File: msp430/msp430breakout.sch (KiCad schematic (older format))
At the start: 18 parts, among them P1 Power, T1 Crystal_Small, X1 Power, X2 Power, X3 Left, X4 Power, X5 Power, X6 Right, X7 Debug

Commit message: a bit of work on the layout
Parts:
- removed X3: Left, Connector_PinHeader_2.54mm:PinHeader_1x06_P2.54mm_Vertical, symbol Connector:Conn_01x06_Male
- removed X6: Right, Connector_PinHeader_2.54mm:PinHeader_1x06_P2.54mm_Vertical, symbol Connector:Conn_01x06_Male
- added X3: Left, Connector_PinHeader_2.54mm:PinHeader_1x05_P2.54mm_Vertical, symbol Connector:Conn_01x05_Male
- added X6: Right, Connector_PinHeader_2.54mm:PinHeader_1x05_P2.54mm_Vertical, symbol Connector:Conn_01x05_Male
- added X8: PWR_L_OOL, Connector_PinHeader_2.54mm:PinHeader_2x02_P2.54mm_Vertical, symbol Connector:Conn_01x04_Male
- added X9: PWR_R_OOL, Connector_PinHeader_2.54mm:PinHeader_2x02_P2.54mm_Vertical, symbol Connector:Conn_01x04_Male
- X7: footprint Connector_Molex:Molex_Micro-Latch_53253-0370_1x03_P2.00mm_Vertical -> Connector_PinHeader_2.54mm:PinHeader_1x03_P2.54mm_Vertical
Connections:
- wire segments 47 -> 79
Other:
- moved on the sheet: X1, X2, X4, X5

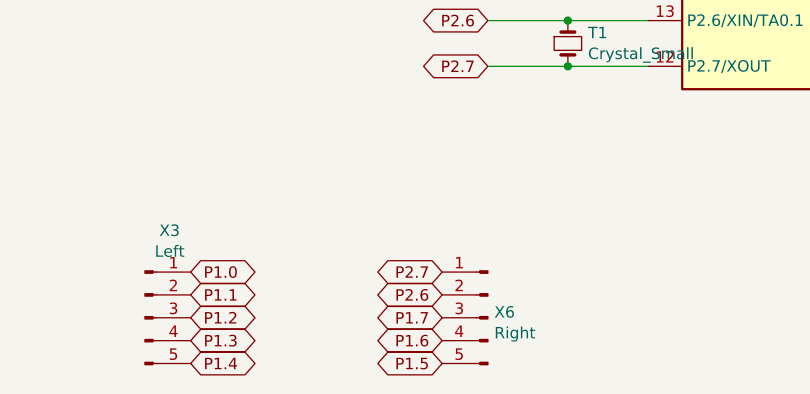
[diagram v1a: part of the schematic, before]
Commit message: increased board size to have planes go around pin headers
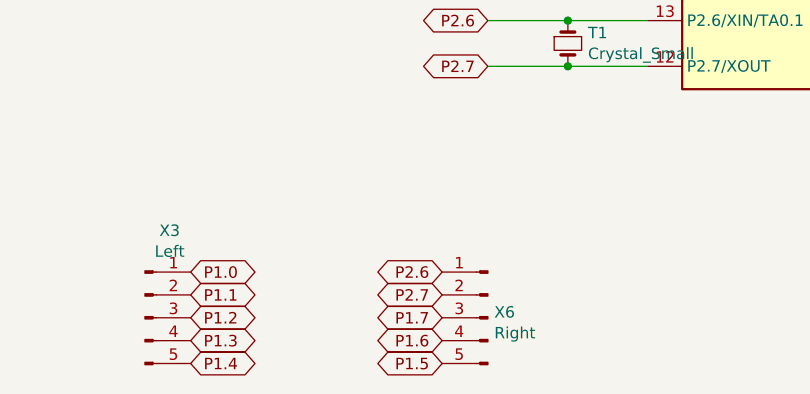
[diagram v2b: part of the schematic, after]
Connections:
- net P2.6: now also X6.1 (Pin_1); no longer X6.2 (Pin_2)
- net P2.7: now also X6.2 (Pin_2); no longer X6.1 (Pin_1)
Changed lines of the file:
@@
 Text GLabel 3300 6500 0    50   BiDi ~ 0
 P1.7
+Text GLabel 3300 6300 0    50   BiDi ~ 0
+P2.6
 Text GLabel 3300 6400 0    50   BiDi ~ 0
-P2.6
-Text GLabel 3300 6300 0    50   BiDi ~ 0
 P2.7
 Text GLabel 5800 4550 2    50   Input ~ 0

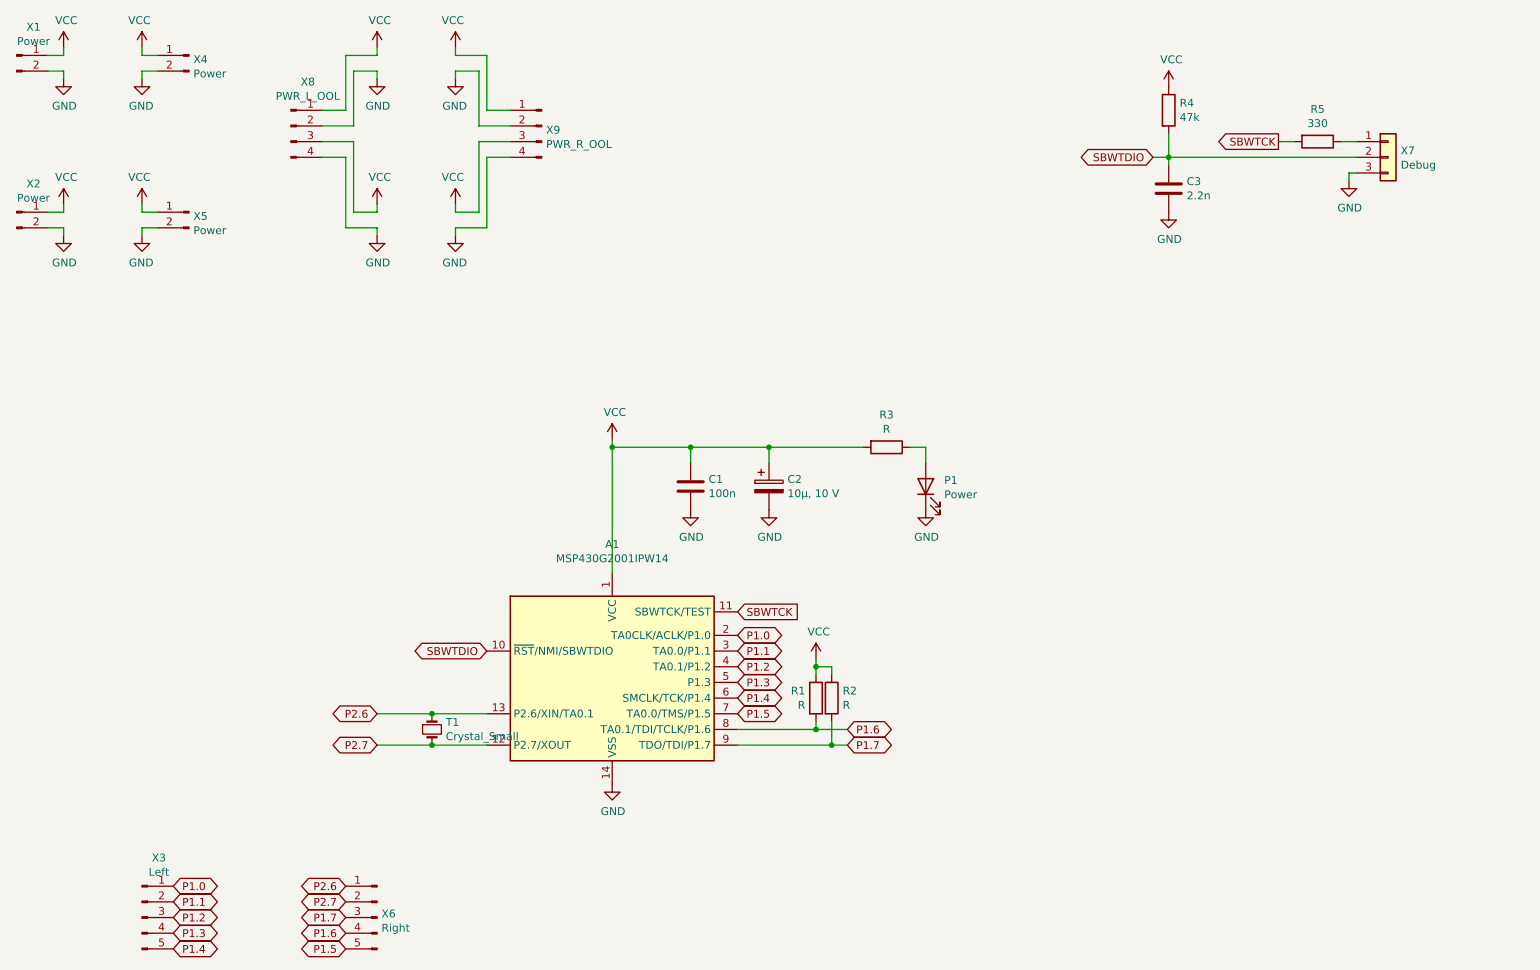
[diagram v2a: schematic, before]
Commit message: added linear regulator
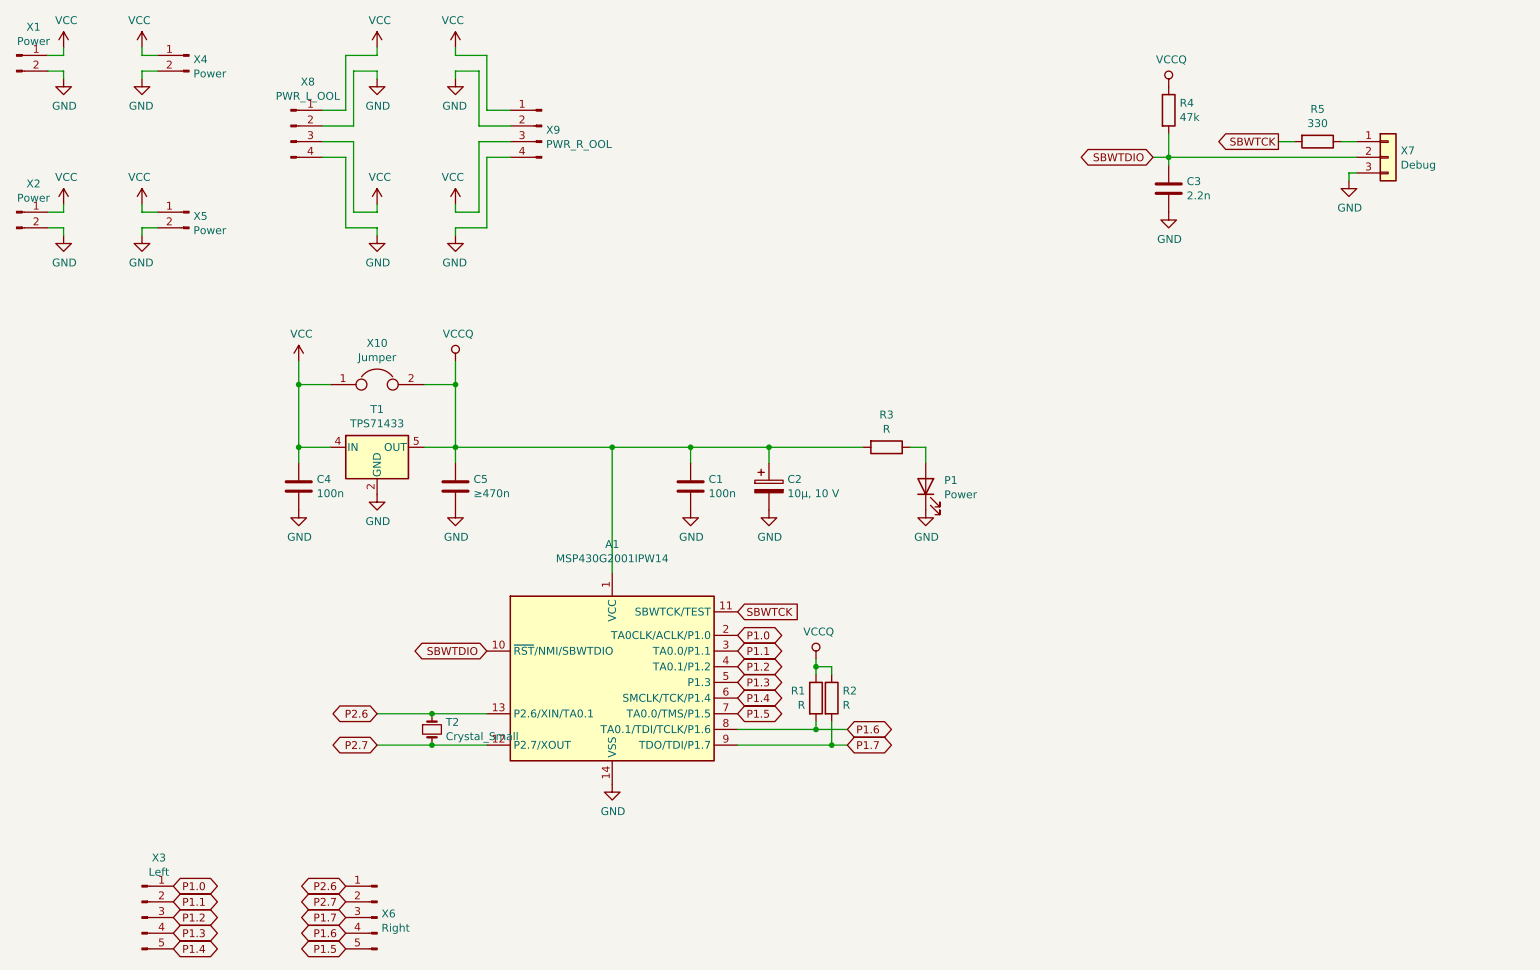
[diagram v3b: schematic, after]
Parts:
- added C4: 100n, Capacitor_SMD:C_0805_2012Metric_Pad1.15x1.40mm_HandSolder, symbol Device:C
- added C5: ≥470n, Capacitor_SMD:C_0805_2012Metric_Pad1.15x1.40mm_HandSolder, symbol Device:C
- added T1: TPS71433, Package_TO_SOT_SMD:SOT-353_SC-70-5, symbol Regulator_Linear:TPS71533__SC70
- added X10: Jumper, symbol Device:Jumper
- renumbered T1 to T2
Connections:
- net GND: now also C4.2, C5.2, T1.2 (GND)
- net VCC: now also C4.1, T1.4 (IN), X10.1; no longer A1.1 (VCC), C1.1, C2.1, R1.1, R2.1, R3.2, R4.1
- new net VCCQ: A1.1 (VCC), C1.1, C2.1, C5.1, R1.1, R2.1, R3.2, R4.1, T1.5 (OUT), X10.2
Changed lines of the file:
@@
-	1    0    0    -1
-$EndComp
-Connection ~ 5000 3500
-Wire Wire Line
-	5000 3450 5000 3500
-$Comp
-L power:VCC #PWR0103
-U 1 1 5E4D6472
-P 5000 3450
-F 0 "#PWR0103" H 5000 3300 50  0001 C CNN
-F 1 "VCC" H 5017 3623 50  0000 C CNN
-F 2 "" H 5000 3450 50  0001 C CNN
-F 3 "" H 5000 3450 50  0001 C CNN
-	1    5000 3450
 	1    0    0    -1
 $EndComp
@@
 	6300 4900 6300 4850
 Connection ~ 6300 4900
-$Comp
-L power:VCC #PWR0116
-U 1 1 5E4EBDF5
-P 6300 4850
-F 0 "#PWR0116" H 6300 4700 50  0001 C CNN
-F 1 "VCC" H 6317 5023 50  0000 C CNN
-F 2 "" H 6300 4850 50  0001 C CNN
-F 3 "" H 6300 4850 50  0001 C CNN
-	1    6300 4850
-	1    0    0    -1
-$EndComp
 Wire Wire Line
 	9350 1550 9250 1550
-$Comp
-L power:VCC #PWR0117
-U 1 1 5E4F1295
-P 8550 1200
-F 0 "#PWR0117" H 8550 1050 50  0001 C CNN
-F 1 "VCC" H 8567 1373 50  0000 C CNN
-F 2 "" H 8550 1200 50  0001 C CNN
-F 3 "" H 8550 1200 50  0001 C CNN
-	1    8550 1200
-	1    0    0    -1
-$EndComp
 Wire Wire Line
 	8450 1650 8550 1650
@@
 	8550 1650 9750 1650
 $Comp
-L Device:Crystal_Small T1
+L Device:Crystal_Small T2
 U 1 1 5E4F5798
 P 3850 5300
-F 0 "T1" V 3804 5388 50  0000 L CNN
+F 0 "T2" V 3804 5388 50  0000 L CNN
 F 1 "Crystal_Small" V 3895 5388 50  0000 L CNN
 F 2 "" H 3850 5300 50  0001 C CNN
@@
 	-1   0    0    -1
 $EndComp
+$Comp
+L Regulator_Linear:TPS71533__SC70 T1
+U 1 1 5E4FAA2B
+P 3500 3500
+F 0 "T1" H 3500 3742 50  0000 C CNN
+F 1 "TPS71433" H 3500 3651 50  0000 C CNN
+F 2 "Package_TO_SOT_SMD:SOT-353_SC-70-5" H 3500 3725 50  0001 C CNN
+F 3 "http://www.ti.com/lit/ds/symlink/tps715.pdf" H 3200 4300 50  0001 C CNN
+	1    3500 3500
+	1    0    0    -1
+$EndComp
+$Comp
+L power:GND #PWR0103
+U 1 1 5E4FBEB1
+P 3500 3800
+F 0 "#PWR0103" H 3500 3550 50  0001 C CNN
+F 1 "GND" H 3505 3627 50  0000 C CNN
+F 2 "" H 3500 3800 50  0001 C CNN
+F 3 "" H 3500 3800 50  0001 C CNN
+	1    3500 3800
+	1    0    0    -1
+$EndComp
+$Comp
+L Device:C C4
+U 1 1 5E4FC63E
+P 3000 3750
+F 0 "C4" H 3115 3796 50  0000 L CNN
+F 1 "100n" H 3115 3705 50  0000 L CNN
+F 2 "Capacitor_SMD:C_0805_2012Metric_Pad1.15x1.40mm_HandSolder" H 3038 3600 50  0001 C CNN
+F 3 "~" H 3000 3750 50  0001 C CNN
+	1    3000 3750
+	1    0    0    -1
+$EndComp
+$Comp
+L Device:C C5
+U 1 1 5E4FCCBF
+P 4000 3750
+F 0 "C5" H 4115 3796 50  0000 L CNN
+F 1 "≥470n" H 4115 3705 50  0000 L CNN
+F 2 "Capacitor_SMD:C_0805_2012Metric_Pad1.15x1.40mm_HandSolder" H 4038 3600 50  0001 C CNN
+F 3 "~" H 4000 3750 50  0001 C CNN
+	1    4000 3750
+	1    0    0    -1
+$EndComp
+Wire Wire Line
+	3800 3500 4000 3500
+Wire Wire Line
+	4000 3500 4000 3600
+Wire Wire Line
+	3200 3500 3000 3500
+Wire Wire Line
+	3000 3500 3000 3600
+$Comp
+L power:GND #PWR0126
+U 1 1 5E5010F7
+P 3000 3900
+F 0 "#PWR0126" H 3000 3650 50  0001 C CNN
+F 1 "GND" H 3005 3727 50  0000 C CNN
+F 2 "" H 3000 3900 50  0001 C CNN
+F 3 "" H 3000 3900 50  0001 C CNN
+	1    3000 3900
+	1    0    0    -1
+$EndComp
+$Comp
+L power:GND #PWR0127
+U 1 1 5E501339
+P 4000 3900
+F 0 "#PWR0127" H 4000 3650 50  0001 C CNN
+F 1 "GND" H 4005 3727 50  0000 C CNN
+F 2 "" H 4000 3900 50  0001 C CNN
+F 3 "" H 4000 3900 50  0001 C CNN
+	1    4000 3900
+	1    0    0    -1
+$EndComp
+$Comp
+L power:VCC #PWR0128
+U 1 1 5E503C52
+P 3000 2950
+F 0 "#PWR0128" H 3000 2800 50  0001 C CNN
+F 1 "VCC" H 3017 3123 50  0000 C CNN
+F 2 "" H 3000 2950 50  0001 C CNN
+F 3 "" H 3000 2950 50  0001 C CNN
+	1    3000 2950
+	1    0    0    -1
+$EndComp
+Connection ~ 3000 3500
+Wire Wire Line
+	4000 3500 5000 3500
+Connection ~ 4000 3500
+Connection ~ 5000 3500
+Wire Wire Line
+	3000 2950 3000 3100
+$Comp
+L Device:Jumper X10
+U 1 1 5E50AFA6
+P 3500 3100
+F 0 "X10" H 3500 3364 50  0000 C CNN
+F 1 "Jumper" H 3500 3273 50  0000 C CNN
+F 2 "" H 3500 3100 50  0001 C CNN
+F 3 "~" H 3500 3100 50  0001 C CNN
+	1    3500 3100
+	1    0    0    -1
+$EndComp
+Wire Wire Line
+	3200 3100 3000 3100
+Connection ~ 3000 3100
+Wire Wire Line
+	3000 3100 3000 3500
+Wire Wire Line
+	3800 3100 4000 3100
+Wire Wire Line
+	4000 3100 4000 3500
+Wire Wire Line
+	4000 2950 4000 3100
+Connection ~ 4000 3100
+$Comp
+L power:VCCQ #PWR0129
+U 1 1 5E577B5D
+P 4000 2950
+F 0 "#PWR0129" H 4000 2800 50  0001 C CNN
+F 1 "VCCQ" H 4017 3123 50  0000 C CNN
+F 2 "" H 4000 2950 50  0001 C CNN
+F 3 "" H 4000 2950 50  0001 C CNN
+	1    4000 2950
+	1    0    0    -1
+$EndComp
+$Comp
+L power:VCCQ #PWR0117
+U 1 1 5E579A8C
+P 8550 1200
+F 0 "#PWR0117" H 8550 1050 50  0001 C CNN
+F 1 "VCCQ" H 8567 1373 50  0000 C CNN
+F 2 "" H 8550 1200 50  0001 C CNN
+F 3 "" H 8550 1200 50  0001 C CNN
+	1    8550 1200
+	1    0    0    -1
+$EndComp
+$Comp
+L power:VCCQ #PWR?
+U 1 1 5E57A4E6
+P 6300 4850
+F 0 "#PWR?" H 6300 4700 50  0001 C CNN
+F 1 "VCCQ" H 6317 5023 50  0000 C CNN
+F 2 "" H 6300 4850 50  0001 C CNN
+F 3 "" H 6300 4850 50  0001 C CNN
+	1    6300 4850
+	1    0    0    -1
+$EndComp
 $EndSCHEMATC

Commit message: modified for better usability with FET
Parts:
- removed X4, X5: Power, Connector_PinHeader_2.54mm:PinHeader_1x02_P2.54mm_Vertical, symbol Connector:Conn_01x02_Male
- removed X7: Debug, Connector_PinHeader_2.54mm:PinHeader_1x03_P2.54mm_Vertical, symbol Connector_Generic:Conn_01x03
- removed X9: PWR_R_OOL, Connector_PinHeader_2.54mm:PinHeader_2x02_P2.54mm_Vertical, symbol Connector:Conn_01x04_Male
- added X10, X9: backchannel UART, Connector_PinHeader_2.54mm:PinHeader_1x02_P2.54mm_Vertical, symbol Device:Jumper
- added X7: Spy-Bi-Wire, Connector_IDC:IDC-Header_2x07_P2.54mm_Vertical, symbol Connector_Generic:Conn_02x07_Odd_Even
- added X8: power by tool, Connector_PinHeader_2.54mm:PinHeader_1x02_P2.54mm_Vertical, symbol Device:Jumper
- X1, X2: value Power -> power
- X4: renamed from X8; value PWR_L_OOL -> power
- X5: renamed from X10; value Jumper -> bus is 3.3V; footprint (none) -> Connector_PinHeader_2.54mm:PinHeader_1x02_P2.54mm_Vertical
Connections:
- net VCCQ is gone; now on net VCC: A1.1 (VCC), C1.1, C2.1, C5.1, R1.1, R2.1, R3.2, R4.1, T1.5 (OUT), X5.2
- net GND: now also X7.9 (Pin_9)
- net SBWTDIO: now also X7.1 (Pin_1)
- net VCC: now also X7.4 (Pin_4), X8.2; no longer C4.1, T1.4 (IN), X1.1 (Pin_1), X2.1 (Pin_1), X4.1 (Pin_1), X4.3 (Pin_3), X5.1
- net at R5.1: now also X7.7 (Pin_7)
- new net +3V3: X7.2 (Pin_2), X8.1
- new net +5V: C4.1, T1.4 (IN), X1.1 (Pin_1), X2.1 (Pin_1), X4.1 (Pin_1), X4.3 (Pin_3), X5.1
- new net UART_RXD: X10.2, X7.14 (Pin_14)
- new net UART_TXD: X7.12 (Pin_12), X9.2
- no-connect marks 0 -> 7
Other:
- note added: "GND"
- note added: "N/C"
- note added: "RST"
- note added: "Really needed? Probe\npulls this up already."
- note added: "TCK"
- note added: "TDI/VPP"
- note added: "TDO/TDI"
- note added: "TEST/VPP"
- note added: "TMS"
- note added: "UART_CTS/SPI_CLK/I2C_SCL"
- note added: "UART_RTS"
- note added: "UART_RXD/SPI_SIMO"
- note added: "UART_TXD/SPI_SOMI/I2C_SDA"
- note added: "VCC_TARGET"
- note added: "VCC_TOOL"
- moved on the sheet: C3, R4, R5, T2, X3, X4, X6

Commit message: finished rev.0
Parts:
- removed R1, R2: R, Resistor_SMD:R_0805_2012Metric_Pad1.15x1.40mm_HandSolder, symbol Device:R
- removed X5: bus is 3.3V, Connector_PinHeader_2.54mm:PinHeader_1x02_P2.54mm_Vertical, symbol Device:Jumper
- C1: renamed from C4; value 100n -> 100 nF
- C2: renamed from C5; value ≥470n -> ≥470 nF
- C3: renamed from C1; value 100n -> 100 nF
- C4: renamed from C2; value 10µ, 10 V -> 10 µF, 10 V
- C5: renamed from C3; value 2.2n -> 2.2 nF
- X8: renamed from X9; footprint Connector_PinHeader_2.54mm:PinHeader_1x02_P2.54mm_Vertical -> Resistor_SMD:R_0805_2012Metric_Pad1.15x1.40mm_HandSolder
- X9: renamed from X10; footprint Connector_PinHeader_2.54mm:PinHeader_1x02_P2.54mm_Vertical -> Resistor_SMD:R_0805_2012Metric_Pad1.15x1.40mm_HandSolder
- renumbered R3 to R1, R4 to R2, R5 to R3, X4 to X3, X3 to X4, X6 to X5, X7 to X6, X8 to X7
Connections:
- net GND: now also R1.1; no longer P1.1 (K)
- net P1.1: now also X9.1
- net P1.2: now also X8.1
- net VCC: now also P1.2 (A); no longer R1.2
- new net: P1.1 (K), R1.2
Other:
- moved on the sheet: P1, R1, X5

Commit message: comitting current state
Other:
- note removed: "Really needed? Probe\npulls this up already."
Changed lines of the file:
@@
 Wire Wire Line
 	7050 1700 8550 1700
-Text Notes 7250 1300 0    50   ~ 0
-Really needed? Probe\npulls this up already.
 $Comp
 L Device:R R2
